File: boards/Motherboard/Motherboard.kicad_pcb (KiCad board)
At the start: 2 copper layers, 184.1 x 83.8 mm, 157 parts, among them J201 DIGILENT_VHDCI_CONN, J601 USB, P601 ICSP, P602 SPI2, P701 SLOT-A, P702 SLOT-B, P703 SLOT-C, P704 SLOT-D, P705 SLOT-E, U401 24AA014, U501 ROE-0505S, U601 SI8660, U602 SI8660, U603 SI8660, U604 SI8660, U605 SI8660, U606 SI8660, U607 PIC18F85J94, U608 AAT3221IGV-3.3-T1, X601 XTAL

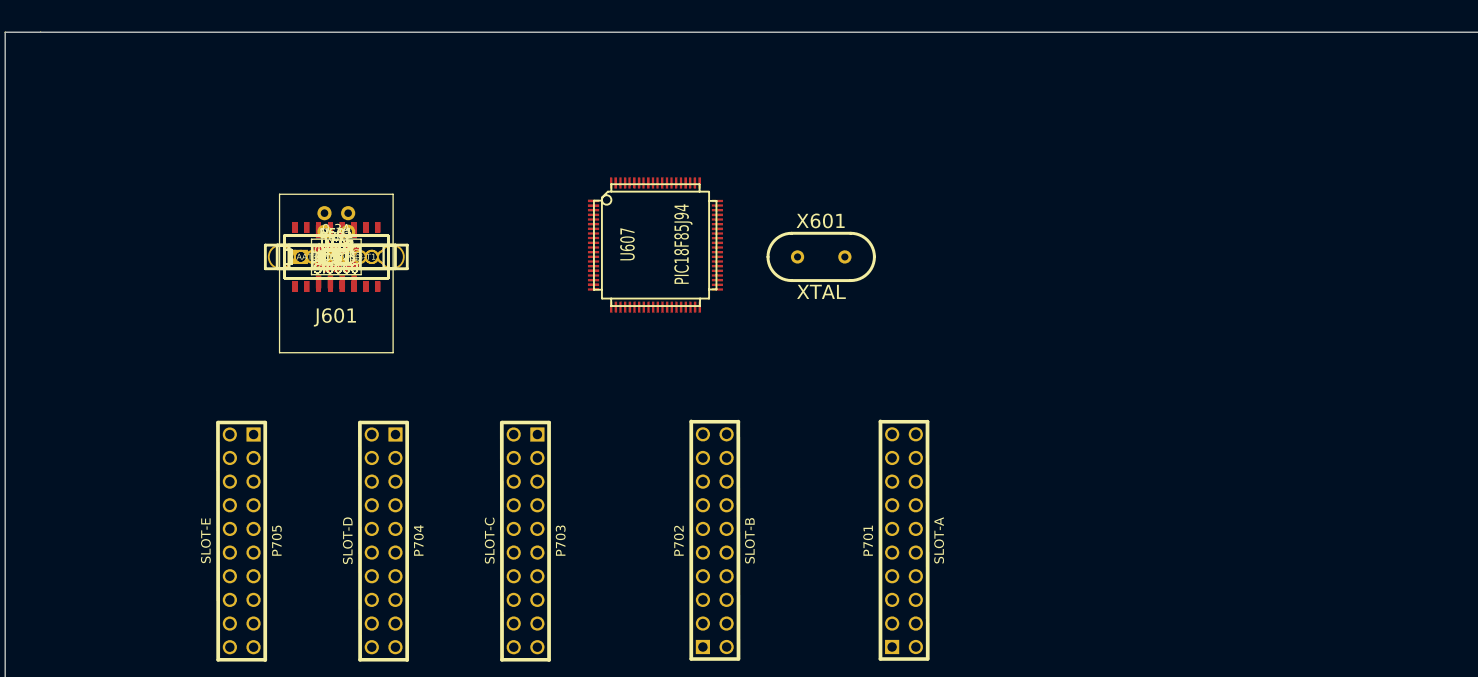
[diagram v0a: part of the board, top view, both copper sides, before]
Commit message: Motherboard PCB components all spread out
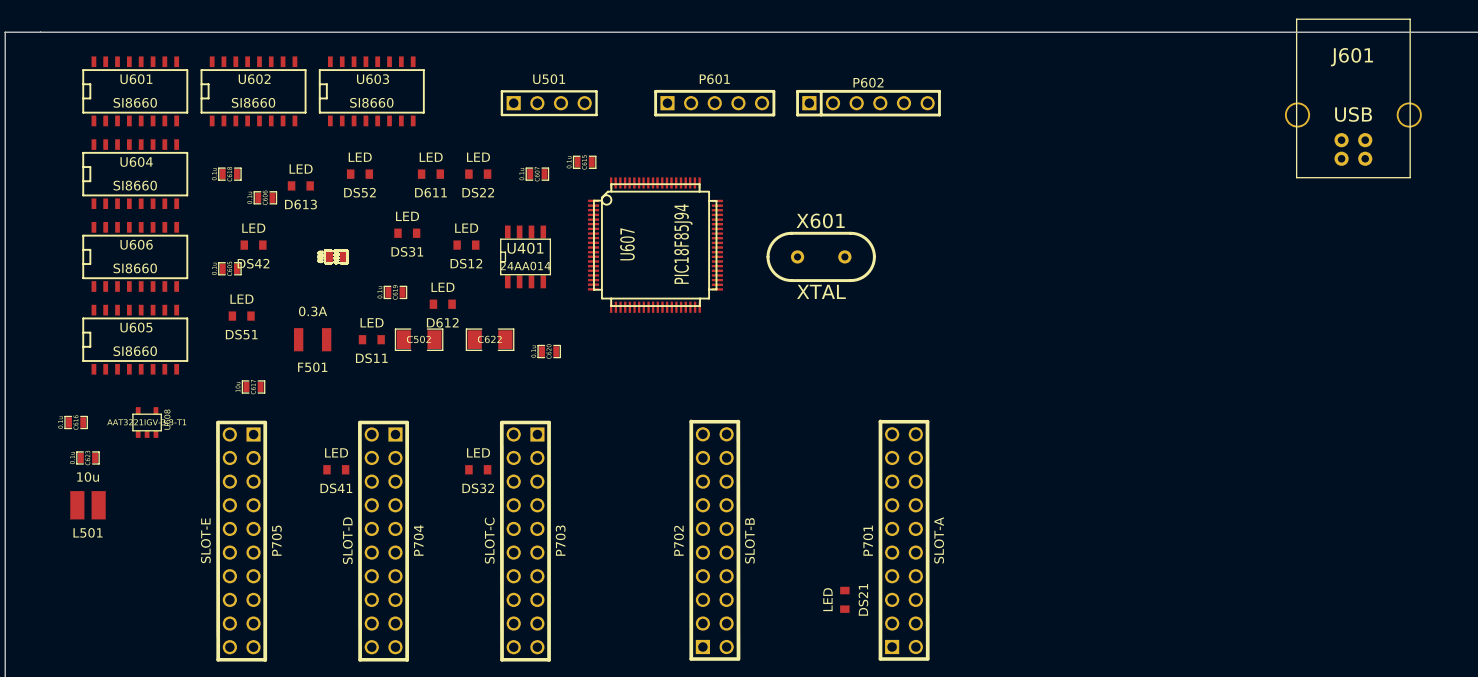
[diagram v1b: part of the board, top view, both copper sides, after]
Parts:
- L501: footprint SM0603_Capa -> Murata_8200_SMD
- moved J601 110.3 mm to (167.6, 35.6), turned to 180 degrees
- moved DS21 65.9 mm to (113.0, 87.6)
- moved P602 59.5 mm to (115.6, 34.3)
- moved P601 43.9 mm to (99.1, 34.3)
- moved L501 37.7 mm to (31.8, 77.5)
- moved C623 34.3 mm to (31.8, 72.4)
- moved C616 33.1 mm to (30.5, 68.6)
- moved C615 28.5 mm to (85.1, 40.6)
- moved U501 28.2 mm to (81.3, 34.3)
- moved U601 28.0 mm to (36.8, 33.0)
- moved DS32 27.5 mm to (73.7, 73.7)
- moved U608 27.0 mm to (38.1, 68.6)
- moved C620 25.0 mm to (81.3, 61.0)
- moved C607 23.3 mm to (80.0, 41.9)
- moved U604 23.3 mm to (36.8, 41.9)
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
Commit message: Components coagulated and arranged in motherboard PCB
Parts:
- removed P701: SLOT-A, pin_array_10x2
- removed P702: SLOT-B, pin_array_10x2
- removed P703: SLOT-C, pin_array_10x2
- removed P704: SLOT-D, pin_array_10x2
- removed P705: SLOT-E, pin_array_10x2
- added Atlys_screw_hole: VAL**, Atlys_screw_hole, F.Cu at (33.8, 146.8)
- added Atlys_screw_hole: VAL**, Atlys_screw_hole, F.Cu at (33.8, 261.2)
- added Atlys_screw_hole: VAL**, Atlys_screw_hole, F.Cu at (244.2, 146.8)
- added Atlys_screw_hole: VAL**, Atlys_screw_hole, F.Cu at (244.2, 261.2)
- added X701: SLOT 1, dboard_slot, F.Cu at (210.0, 220.0)
- added X702: SLOT 2, dboard_slot, F.Cu at (170.0, 220.0)
- added X703: SLOT 3, dboard_slot, F.Cu at (130.0, 220.0)
- added X704: SLOT 4, dboard_slot, F.Cu at (90.0, 220.0)
- added X705: SLOT 5, dboard_slot, F.Cu at (50.0, 220.0)
- J201: value DIGILENT_VHDCI_CONN -> DIGILENT VHDCI
- R688, R689, R690, RS11, RS12, RS21, RS22, RS31, RS32, RS41, RS42, RS51, RS52: value 330 -> 680
- U605, U606: value SI8660 -> SI8630/SI8660
- moved R201 222.6 mm to (240.9, 178.2)
- moved C201 219.1 mm to (236.6, 178.2)
- moved L501 217.8 mm to (235.9, 153.2), turned to 270 degrees
- moved C623 212.9 mm to (225.8, 160.1), turned to 270 degrees
- moved U608 203.9 mm to (222.1, 156.7), turned to 270 degrees
- moved R691 197.5 mm to (225.8, 155.7), turned to 270 degrees
- moved R641 196.9 mm to (221.9, 160.6)
- moved C502 195.5 mm to (235.9, 158.6), turned to 270 degrees
- moved C501 195.3 mm to (225.2, 152.3), turned to 180 degrees
- moved F501 195.1 mm to (230.4, 147.0), turned to 180 degrees
- moved U501 192.7 mm to (230.7, 156.1), turned to 90 degrees
- moved R402 176.3 mm to (188.6, 169.7), turned to 180 degrees
- moved R401 175.0 mm to (188.6, 167.7), turned to 180 degrees
- moved C622 172.6 mm to (221.4, 150.9), turned to 90 degrees
- moved C614 169.9 mm to (188.1, 160.5)
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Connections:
- C602 pad 1: N-00000180 (its old number) -> N-00000181
- C606 pad 1: N-00000179 -> N-00000177
- C610 pad 1: N-00000177 -> N-00000178
- C611 pad 1: N-00000178 -> N-00000179
- R608 pad 2: N-00000180 (its old number) -> N-00000181
- R609 pad 2: N-00000111 -> N-00000110
- R610 pad 2: N-00000110 -> N-00000109
- R611 pad 2: N-00000109 -> N-00000108
- R612 pad 2: N-00000108 -> N-00000134
- R613 pad 2: N-00000107 (its old number) -> N-00000150
- R614 pad 2: N-00000112 (its old number) -> N-00000111
- R616 pad 2: N-00000129 -> N-00000126
- R617 pad 2: N-00000128 -> N-00000125
- R618 pad 2: N-00000127 -> N-00000124
- R630 pad 1: N-00000126 -> N-00000123
- R631 pad 1: N-00000125 -> N-00000117
- R632 pad 1: N-00000123 -> N-00000122
- R633 pad 1: N-00000122 -> N-00000121
- R635 pad 1: N-00000121 -> N-00000120
- R636 pad 1: N-00000179 -> N-00000177
- R637 pad 1: N-00000120 -> N-00000119
- R638 pad 1: N-00000119 -> N-00000118
- R639 pad 1: N-00000124 -> N-00000137
- R651 pad 2: N-00000138 -> N-00000136
- R652 pad 2: N-00000137 -> N-00000135
- R653 pad 2: N-00000136 -> N-00000127
- R654 pad 2: N-00000130 -> N-00000133
- R655 pad 2: N-00000135 -> N-00000132
- R656 pad 2: N-00000134 -> N-00000131
- R658 pad 2: N-00000133 -> N-00000130
- R659 pad 2: N-00000132 -> N-00000129
- R660 pad 2: N-00000131 -> N-00000128
- R664 pad 1: N-00000177 -> N-00000178
- R665 pad 1: N-00000139 -> N-00000138
- R666 pad 1: N-00000140 -> N-00000139
- R667 pad 1: N-00000141 -> N-00000140
- R668 pad 1: N-00000142 -> N-00000141
- R669 pad 1: N-00000143 -> N-00000142
- R670 pad 1: N-00000144 (its old number) -> N-00000143
- R671 pad 1: N-00000178 -> N-00000179
- R679 pad 1: N-00000157 -> N-00000159
- R680 pad 1: N-00000158 -> N-00000160
- R681 pad 1: N-00000159 -> N-00000161
- U602 pad 1: N-00000180 (its old number) -> N-00000176
- U602 pad 10: N-00000121 -> N-00000143
- U602 pad 11: N-00000172 -> N-00000142
- U602 pad 12: N-00000122 -> N-00000141
- U602 pad 13: N-00000123 -> N-00000140
- U602 pad 14: N-00000125 -> N-00000139
- U602 pad 15: N-00000126 -> N-00000138
- U602 pad 16: N-00000183 -> N-00000178
- U602 pad 2: N-00000111 -> N-00000151
- U602 pad 3: N-00000110 -> N-00000152
- U602 pad 4: N-00000109 -> N-00000153
- U602 pad 5: N-00000108 -> N-00000154
- U602 pad 6: N-00000107 (its old number) -> N-00000155
- U602 pad 7: N-00000112 (its old number) -> N-00000156
- U602 pad 8: GND -> GND_ISO
- U602 pad 9: GND_ISO -> GND
- U603 pad 1: N-00000184 -> N-00000181
- U603 pad 10: (no net) -> N-00000120
- U603 pad 11: (no net) -> N-00000172
- U603 pad 12: (no net) -> N-00000121
- U603 pad 13: N-00000124 -> N-00000122
- U603 pad 14: N-00000119 -> N-00000117
- U603 pad 15: N-00000120 -> N-00000123
- U603 pad 16: N-00000179 -> N-00000183
- U603 pad 2: N-00000129 -> N-00000110
- U603 pad 3: N-00000128 -> N-00000109
- U603 pad 4: N-00000127 -> N-00000108
- U603 pad 5: (no net) -> N-00000134
- U603 pad 6: (no net) -> N-00000150
- U603 pad 7: (no net) -> N-00000111
- U604 pad 1: N-00000176 -> N-00000173
- U604 pad 10: N-00000144 (its old number) -> N-00000101
- U604 pad 11: N-00000143 -> N-00000102
- U604 pad 12: N-00000142 -> N-00000103
- U604 pad 13: N-00000141 -> N-00000104
- U604 pad 14: N-00000140 -> N-00000105
- U604 pad 15: N-00000139 -> N-00000106
- U604 pad 16: N-00000177 -> N-00000179
- U604 pad 2: N-00000151 -> N-00000136
- U604 pad 3: N-00000152 -> N-00000135
- U604 pad 4: N-00000153 -> N-00000127
- U604 pad 5: N-00000154 -> N-00000133
- U604 pad 6: N-00000155 -> N-00000132
- U604 pad 7: N-00000156 -> N-00000131
- U605 pad 1: N-00000173 -> N-00000184
- U605 pad 10: N-00000101 -> (no net)
- U605 pad 11: N-00000102 -> (no net)
- U605 pad 12: N-00000103 -> N-00000137
- U605 pad 13: N-00000104 -> N-00000118
- U605 pad 14: N-00000105 -> N-00000119
- U605 pad 15: N-00000106 -> (no net)
- U605 pad 16: N-00000178 -> N-00000177
- U605 pad 2: N-00000138 -> (no net)
- U605 pad 3: N-00000137 -> N-00000126
- U605 pad 4: N-00000136 -> N-00000125
- U605 pad 5: N-00000130 -> N-00000124
- U605 pad 6: N-00000135 -> (no net)
- U605 pad 7: N-00000134 -> (no net)
- U605 pad 8: GND_ISO -> GND
- U605 pad 9: GND -> GND_ISO
- U606 pad 12: (no net) -> N-00000161
- U606 pad 13: N-00000159 -> N-00000160
- U606 pad 14: N-00000158 -> N-00000159
- U606 pad 15: N-00000157 -> (no net)
- U606 pad 2: N-00000133 -> (no net)
- U606 pad 3: N-00000132 -> N-00000130
- U606 pad 4: N-00000131 -> N-00000129
- U606 pad 5: (no net) -> N-00000128
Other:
- board size 184.1 x 83.8 mm -> 218 x 122 mm

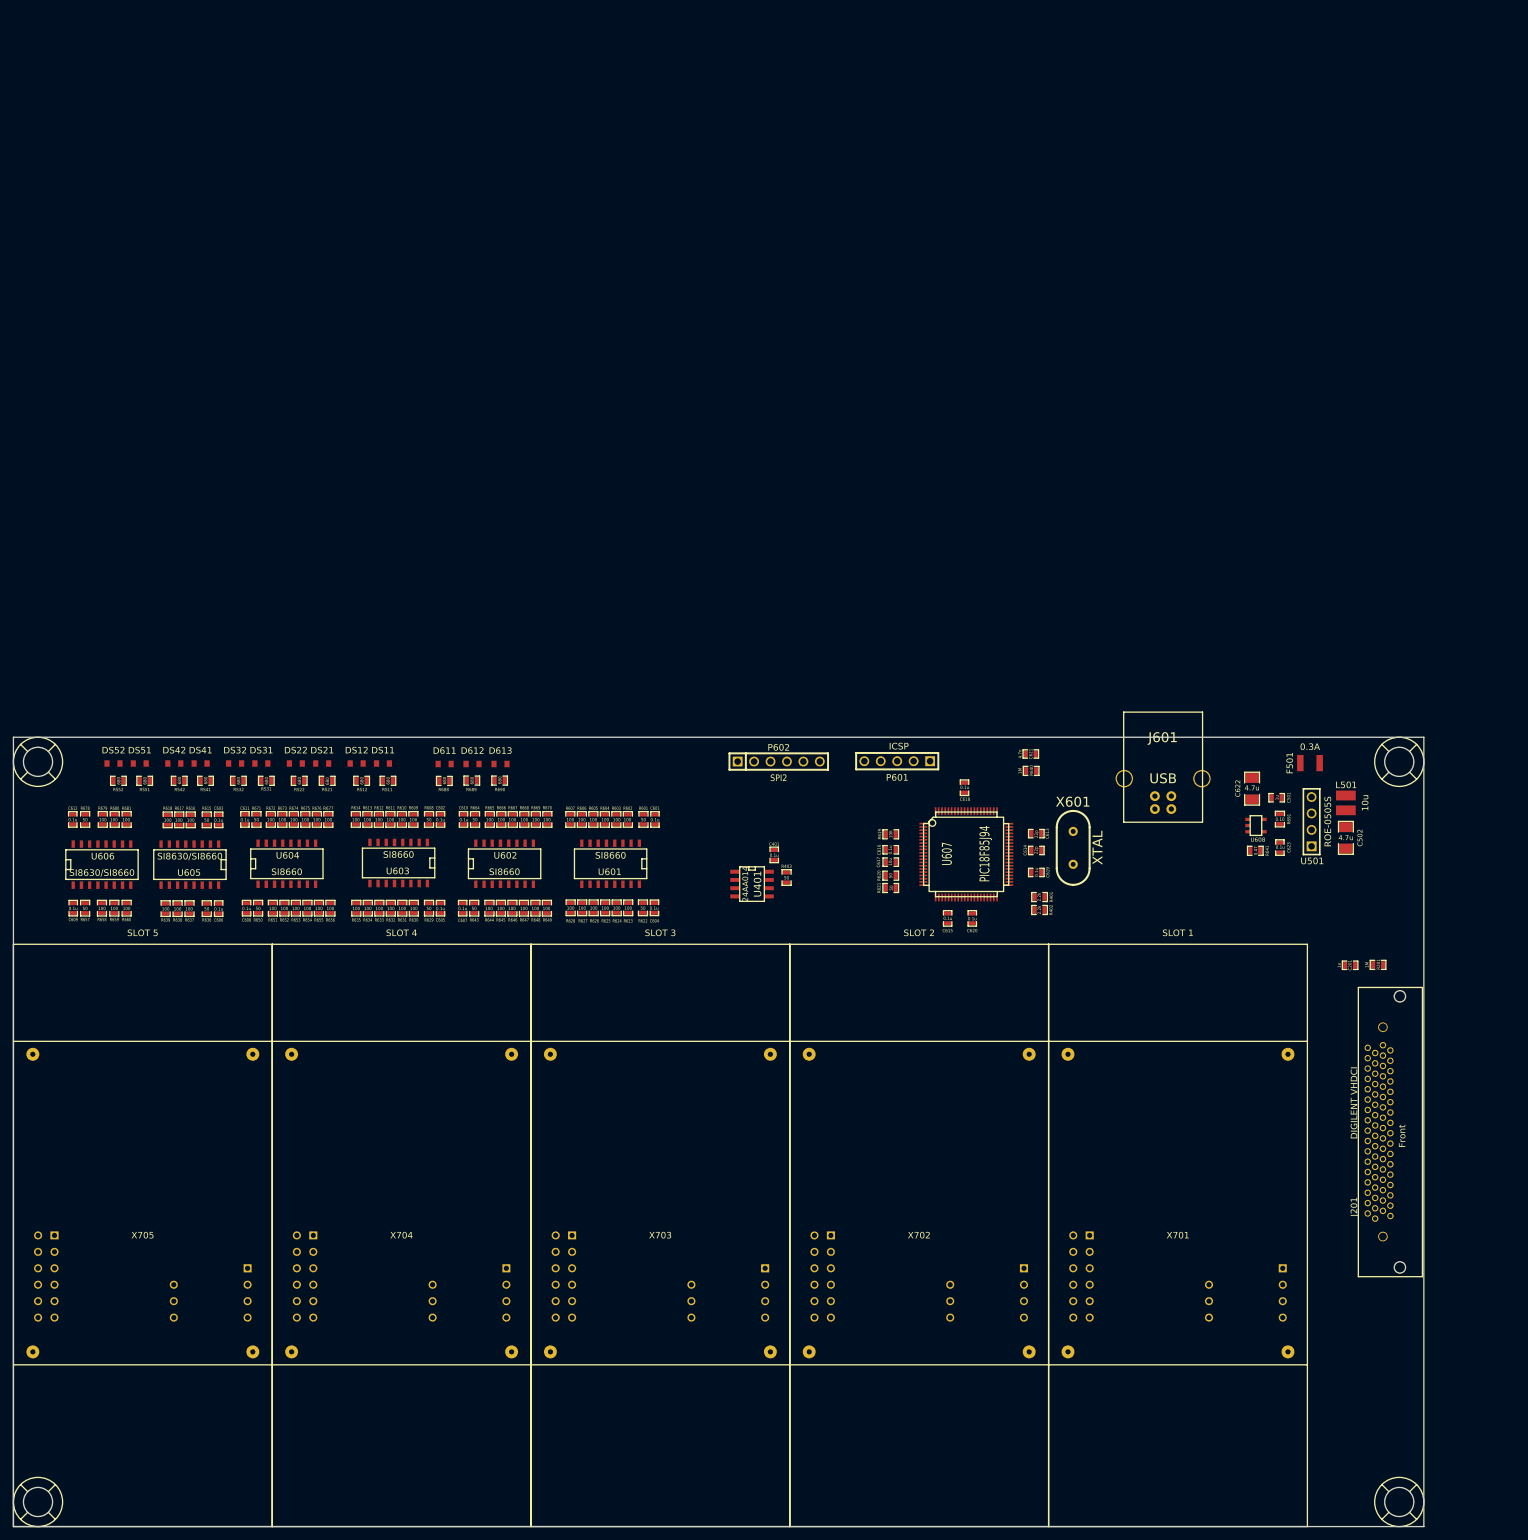
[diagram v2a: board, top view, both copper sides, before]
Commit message: Edited motherboard PCB, changed canvas to A4
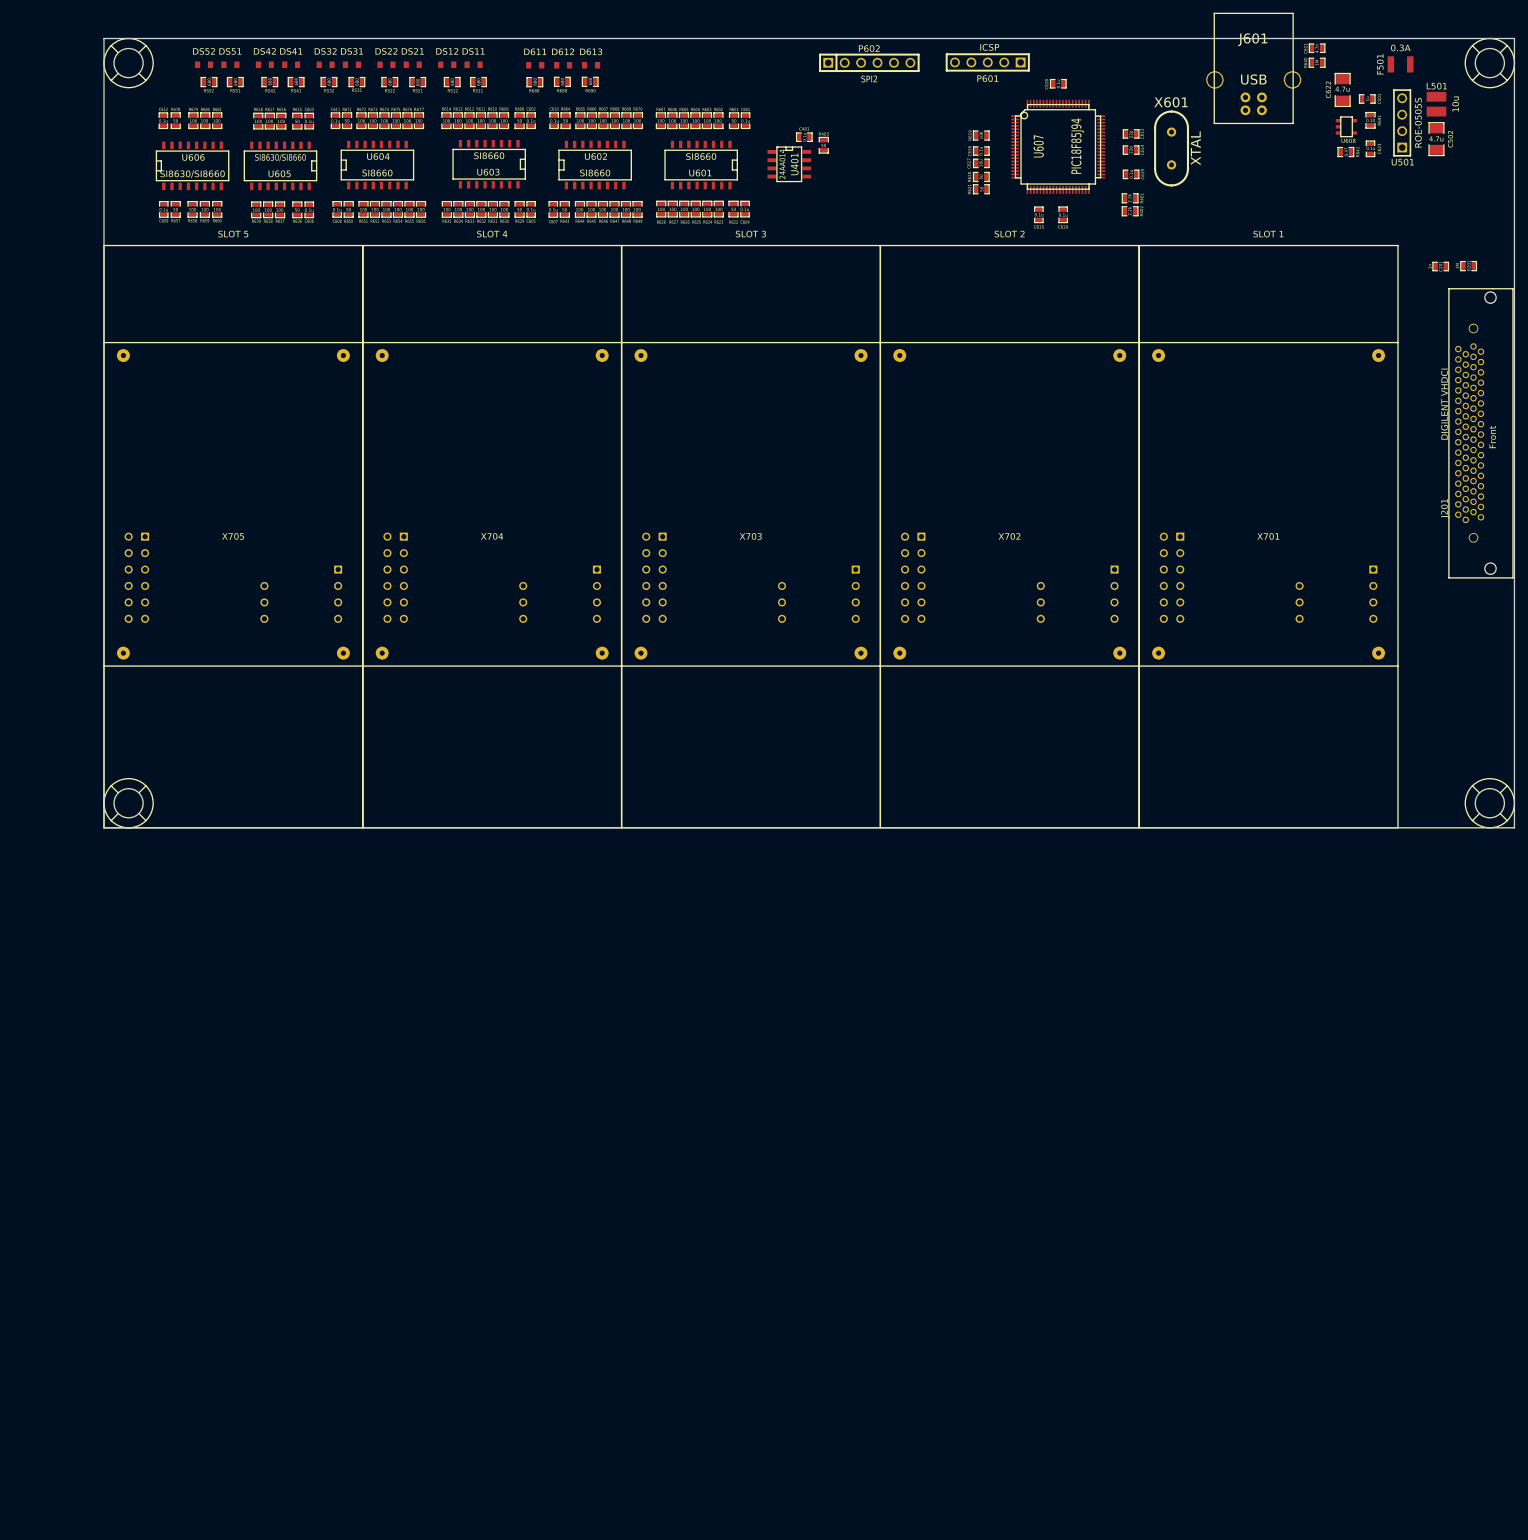
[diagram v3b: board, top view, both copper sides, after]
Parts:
- moved R640 118.0 mm to (231.5, 38.8)
- moved C621 117.7 mm to (231.5, 36.5)
- moved R403 113.3 mm to (155.2, 51.5)
- moved U401 111.4 mm to (149.9, 54.4)
- moved C401 111.0 mm to (152.2, 50.2), turned to 0 degrees
- moved U607 110.3 mm to (191.5, 51.8)
- moved C618 109.8 mm to (191.5, 42.0), turned to 0 degrees
- moved C615 109.7 mm to (188.5, 62.2)
- moved C620 109.7 mm to (192.2, 62.2)
- moved C614 109.2 mm to (202.8, 52.2)
- moved X601 109.2 mm to (209.0, 52.0)
- moved C613 109.1 mm to (202.8, 49.8)
- moved Atlys_screw_hole 108.9 mm to (47.8, 38.8)
- moved Atlys_screw_hole 108.9 mm to (258.2, 38.8)
- moved C502 108.9 mm to (249.9, 50.5)
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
